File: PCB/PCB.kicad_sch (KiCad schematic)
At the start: 14 parts, among them U1 DRV8833PWPR, U2 DRV8833PWPR

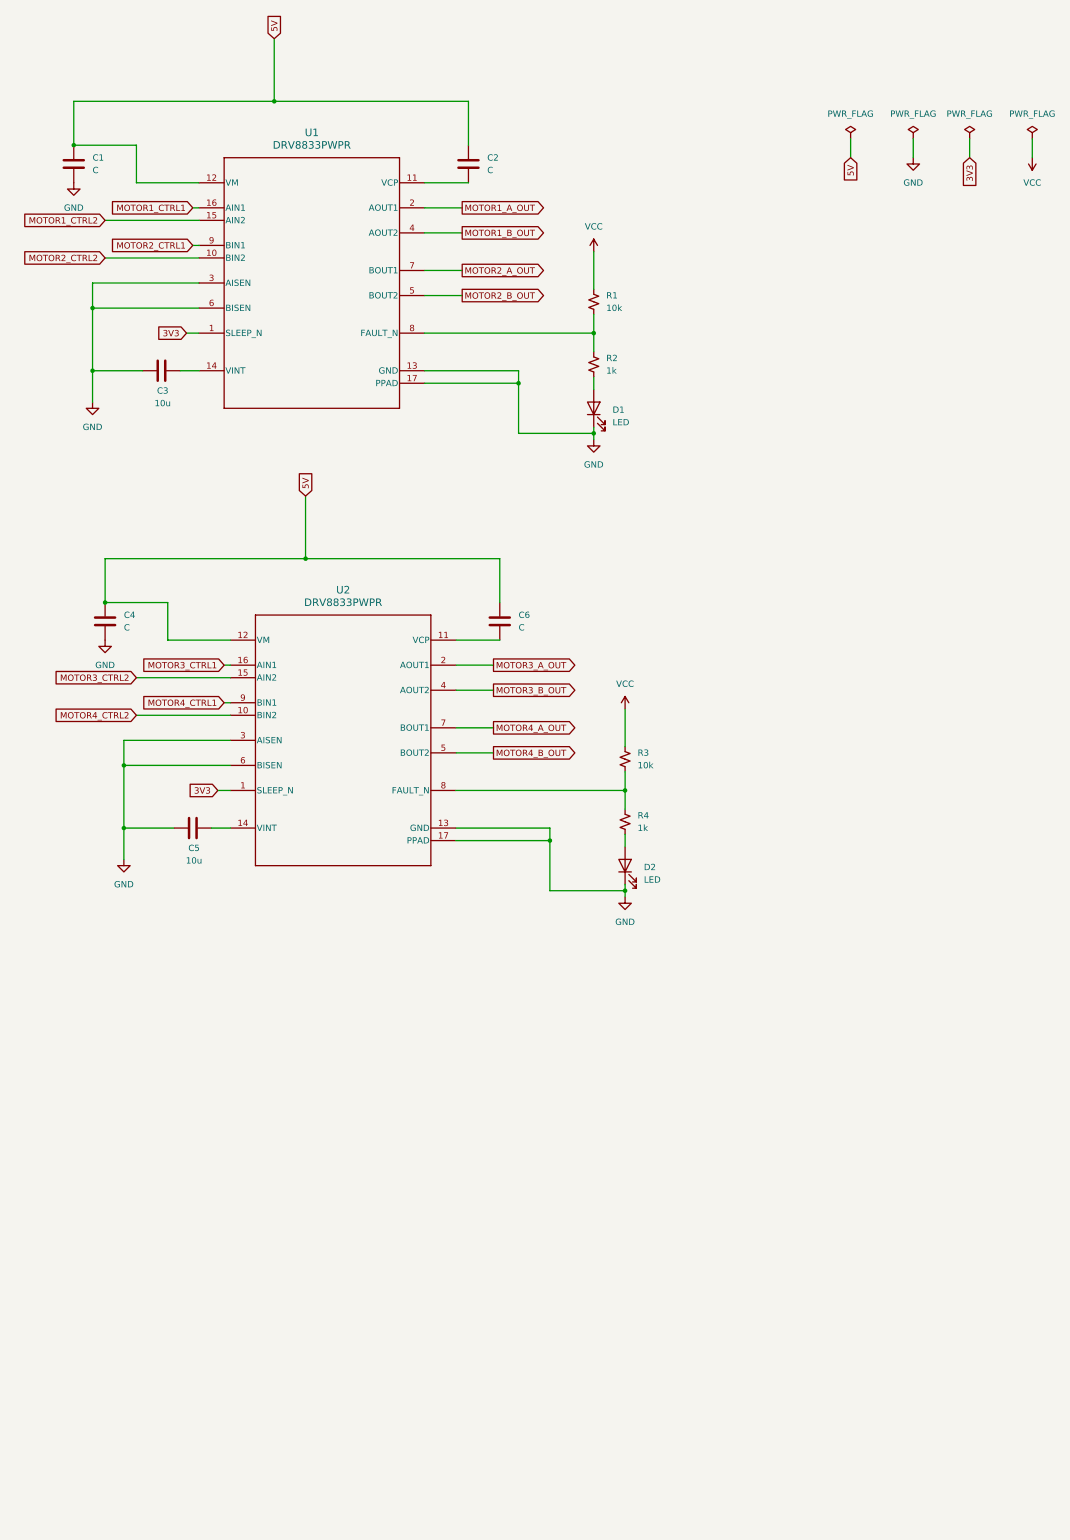
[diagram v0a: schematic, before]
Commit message: External Load Switching
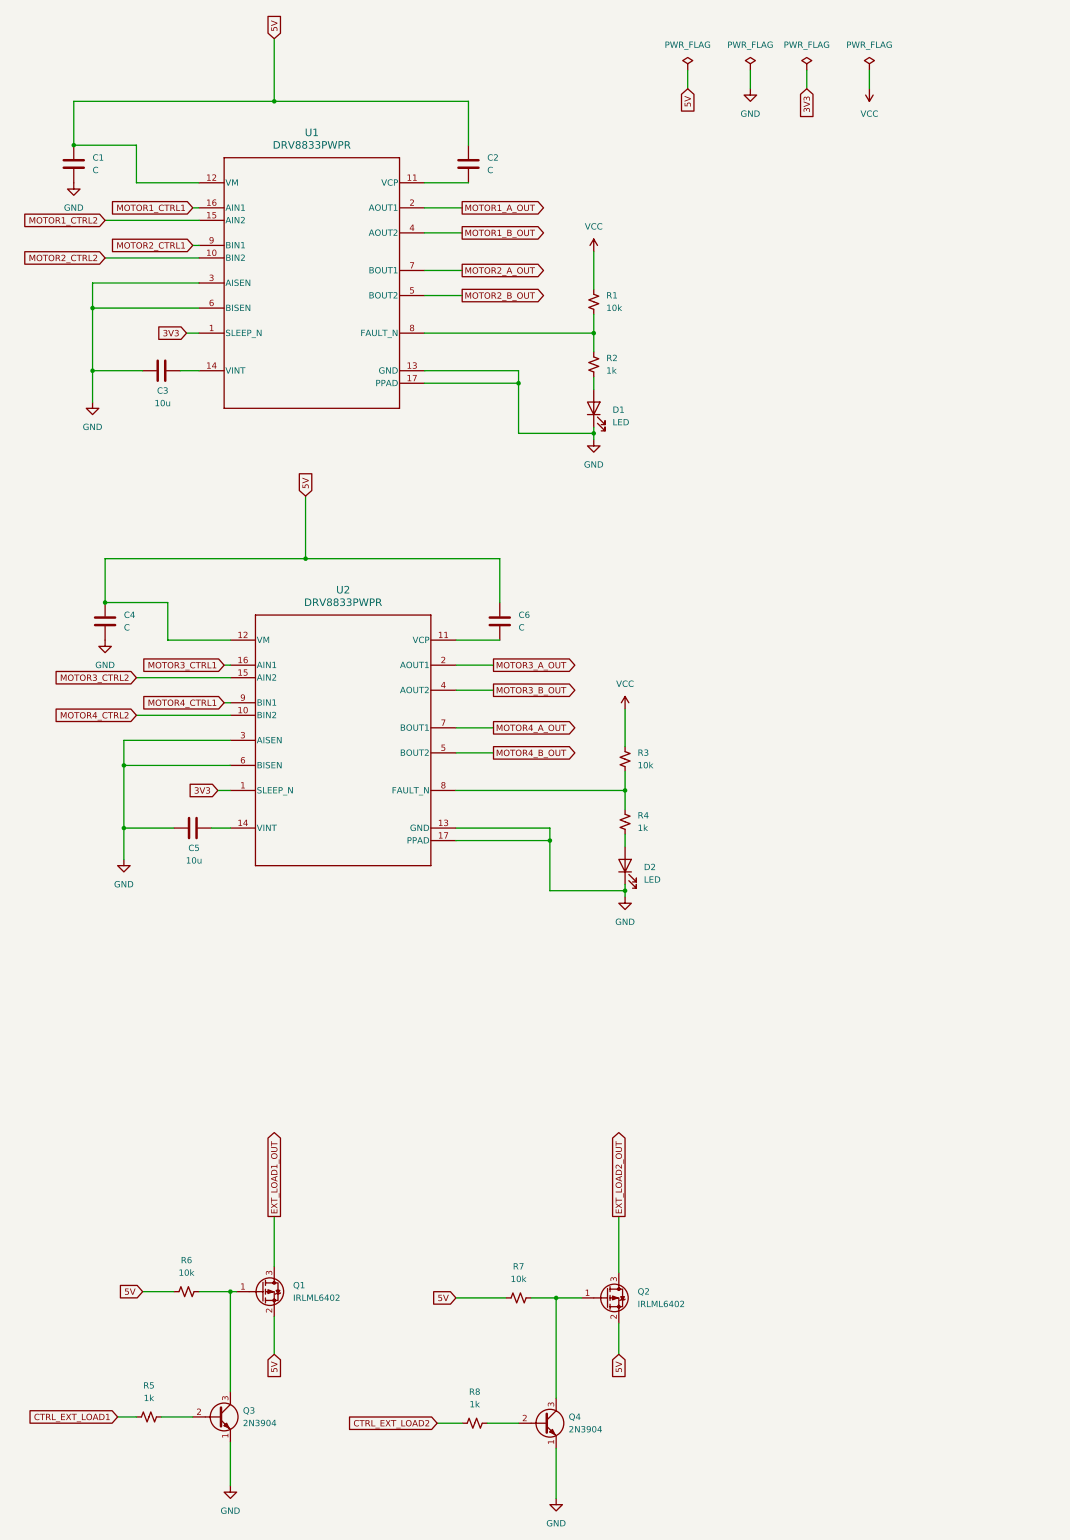
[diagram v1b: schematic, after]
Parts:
- added Q1, Q2: IRLML6402, Package_TO_SOT_SMD:SOT-23, symbol Transistor_FET:IRLML6402
- added Q3, Q4: 2N3904, Package_TO_SOT_THT:TO-92_Inline, symbol Transistor_BJT:2N3904
- added R5, R8: 1k, symbol Device:R_Small_US
- added R6, R7: 10k, symbol Device:R_Small_US
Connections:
- net 5V: now also Q1.2 (S), Q2.2 (S), R6.1, R7.1
- net GND: now also Q3.1 (E), Q4.1 (E)
- new net: Q3.2 (B), R5.2
- new net: Q2.1 (G), Q4.3 (C), R7.2
- new net: Q4.2 (B), R8.1
- new net: Q1.1 (G), Q3.3 (C), R6.2
- new net CTRL_EXT_LOAD1: R5.1
- new net CTRL_EXT_LOAD2: R8.2
- new net EXT_LOAD1_OUT: Q1.3 (D)
- new net EXT_LOAD2_OUT: Q2.3 (D)

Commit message: borderline
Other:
- note added: "The circuit provide two external load switching at 1A."
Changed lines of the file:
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@@
 	(generator_version "9.0")
 	(paper "A1")
+	(text "The circuit provide two external load switching at 1A."
+		(exclude_from_sim no)
+		(at 52.324 243.586 0)
+		(effects
+			(font
+				(size 1.27 1.27)
+				(thickness 0.254)
+				(bold yes)
+			)
+		)
+	)
 	(junction
 		(at 55.88 186.69)
@@
 		)
 	)
+	(polyline
+		(pts
+			(xy 25.4 241.3) (xy 177.8 241.3)
+		)
+		(stroke
+			(width 0)
+			(type default)
+		)
+	)
 	(wire
 		(pts
@@
 		)
 	)
+	(polyline
+		(pts
+			(xy 25.4 241.3) (xy 25.4 342.9)
+		)
+		(stroke
+			(width 0)
+			(type default)
+		)
+	)
 	(wire
 		(pts
@@
 	(wire
 		(pts
-			(xy 59.69 280.67) (xy 66.04 280.67)
+			(xy 55.88 280.67) (xy 66.04 280.67)
 		)
 		(stroke
@@
 		)
 	)
+	(polyline
+		(pts
+			(xy 177.8 241.3) (xy 177.8 342.9)
+		)
+		(stroke
+			(width 0)
+			(type default)
+		)
+	)
 	(wire
 		(pts
@@
 		(pts
 			(xy 52.07 140.97) (xy 64.77 140.97)
+		)
+		(stroke
+			(width 0)
+			(type default)
+		)
+	)
+	(polyline
+		(pts
+			(xy 177.8 342.9) (xy 25.4 342.9)
 		)
 		(stroke
@@
 	(global_label "5V"
 		(shape input)
-		(at 59.69 280.67 180)
+		(at 55.88 280.67 180)
 		(fields_autoplaced yes)
 		(effects
@@
 		)
 		(property "Intersheetrefs" "${INTERSHEET_REFS}"
-			(at 54.4067 280.67 0)
+			(at 50.5967 280.67 0)
 			(effects
 				(font

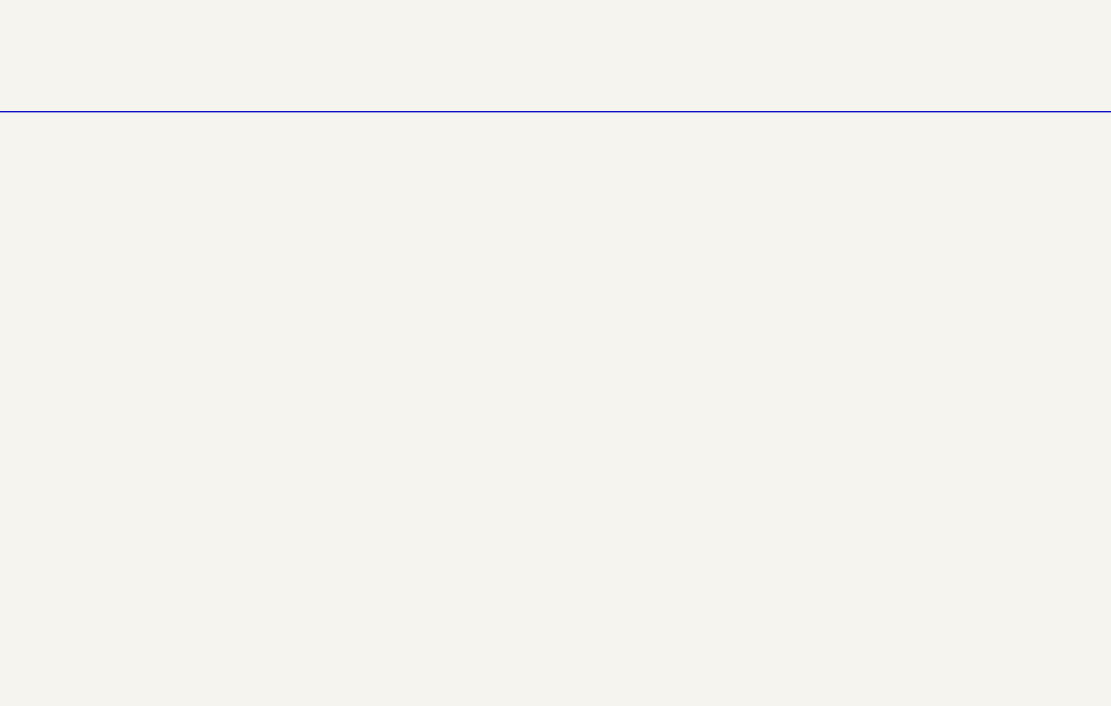
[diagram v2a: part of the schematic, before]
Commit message: Current sensor and conn
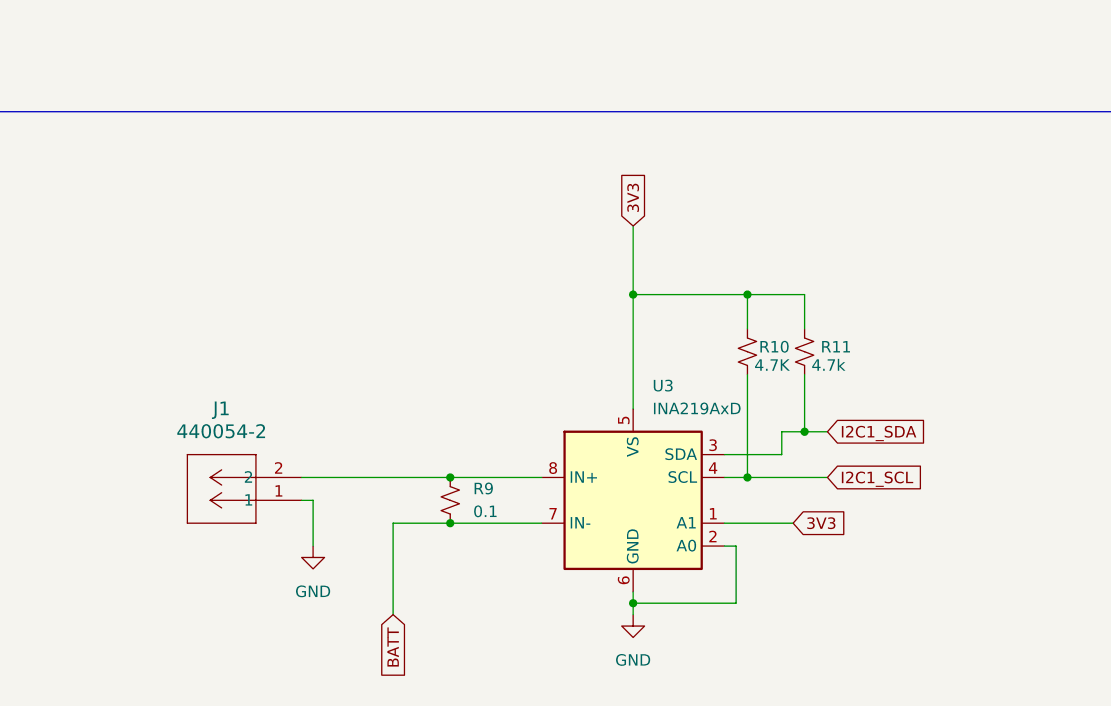
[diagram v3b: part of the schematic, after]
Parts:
- added J1: 440054-2, CONN2_440054-2_TYC, symbol battery conn ul_440054-2:440054-2
- added R10: 4.7K, symbol Device:R_Small_US
- added R11: 4.7k, symbol Device:R_Small_US
- added R9: 0.1, symbol Device:R_Small_US
- added U3: INA219AxD, Package_SO:SOIC-8_3.9x4.9mm_P1.27mm, symbol Sensor_Energy:INA219AxD
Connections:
- net 3V3: now also R10.1, R11.1, U3.1 (A1), U3.5 (VS)
- net GND: now also J1.1, U3.2 (A0), U3.6 (GND)
- new net: J1.2, R9.1, U3.8 (IN+)
- new net BATT: R9.2, U3.7 (IN-)
- new net I2C1_SCL: R10.2, U3.4 (SCL)
- new net I2C1_SDA: R11.2, U3.3 (SDA)

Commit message: Switch added to the schematic
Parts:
- added SW1: SW_SPDT_312, symbol Switch:SW_SPDT_312
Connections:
- net at R9.1, U3.8 (IN+): now also SW1.3 (A); no longer J1.2
- new net: J1.2, SW1.1 (B)
- no-connect marks 0 -> 1
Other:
- note added: "OFF"
- note added: "ON"
- note added: "The switch that will shut down the whole system."
- moved on the sheet: C1, C2, C3, C4, C5, C6, D1, D2, J1, R1, R10, R11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

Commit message: 9V negotiator
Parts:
- added C7: 1u, symbol Device:C
- added J2: USB_C_Receptacle_PowerOnly_6P, symbol Connector:USB_C_Receptacle_PowerOnly_6P
- added R12: 10k, symbol Device:R_Small_US
- added R13: 1k, symbol Device:R_Small_US
- added R14: 6.8k, symbol Device:R_Small_US
- added U4: CH224K, Package_SO:SSOP-10-1EP_3.9x4.9mm_P1mm_EP2.1x3.3mm, symbol Interface_USB:CH224K
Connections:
- net 3V3: now also C7.2, R13.1, U4.1 (VDD)
- net GND: now also C7.1, J2.A12 (GND), J2.B12 (GND), R12.1, R14.1, U4.11 (GND)
- new net: R12.2, U4.8 (VBUS)
- new net: J2.A5 (CC1), U4.7 (CC1)
- new net: J2.B5 (CC2), U4.6 (CC2)
- new net: R14.2, U4.9 (CFG1)
- new net HV: J2.A9 (VBUS), J2.B9 (VBUS), R13.2
- no-connect marks 1 -> 7

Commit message: Lines added
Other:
- note added: "9V negotiator with type C port"
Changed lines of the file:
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@@
+		)
+	)
+	(text "9V negotiator with type C port"
+		(exclude_from_sim no)
+		(at 41.402 436.626 0)
+		(effects
+			(font
+				(size 1.27 1.27)
+			)
 		)
 	)
@@
 		)
 	)
-	(polyline
-		(pts
-			(xy 25.4 127) (xy 177.8 127)
-		)
-		(stroke
-			(width 0)
-			(type default)
-		)
-	)
 	(wire
 		(pts
@@
 		)
 	)
+	(polyline
+		(pts
+			(xy 25.4 120.65) (xy 25.4 127)
+		)
+		(stroke
+			(width 0)
+			(type default)
+		)
+	)
 	(wire
 		(pts
@@
 		)
 	)
+	(polyline
+		(pts
+			(xy 177.8 434.34) (xy 177.8 520.7)
+		)
+		(stroke
+			(width 0)
+			(type default)
+		)
+	)
 	(wire
 		(pts
@@
 		)
 	)
-	(polyline
-		(pts
-			(xy 177.8 123.19) (xy 25.4 123.19)
-		)
-		(stroke
-			(width 0)
-			(type default)
-		)
-	)
 	(wire
 		(pts
@@
 		)
 	)
+	(polyline
+		(pts
+			(xy 25.4 434.34) (xy 177.8 434.34)
+		)
+		(stroke
+			(width 0)
+			(type default)
+		)
+	)
 	(wire
 		(pts
@@
 		)
 	)
+	(polyline
+		(pts
+			(xy 177.8 520.7) (xy 25.4 520.7)
+		)
+		(stroke
+			(width 0)
+			(type default)
+		)
+	)
 	(wire
 		(pts
@@
 		)
 		(stroke
+			(width 0)
+			(type default)
+		)
+	)
+	(polyline
+		(pts
+			(xy 177.8 123.19) (xy 177.8 127)
+		)
+		(stroke
+			(width 0)
+			(type default)
+		)
+	)
+	(polyline
+		(pts
+			(xy 25.4 434.34) (xy 25.4 520.7)
+		)
+		(stroke
